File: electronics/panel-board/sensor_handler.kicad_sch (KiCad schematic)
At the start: 23 parts, among them J1 Load Cell Input, J2 FSR Input, J3 Digital Input, U1 LMV321, U2 INA826

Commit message: Pre LED grid changes
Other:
- note added: "Instrumentation Amplifier for Load Cell Sensor (Typically GML 670, 50kg) - 1kHz cut-off DM filtering. 330x gain. Rail-to-rail output. 470R resistor prevents internal saturation in first stage of inamp due to non rail-to-rail performance internally with CM amplification."
- note removed: "Instrumentation Amplifier for Load Cell Sensor (Typically GML 670, 50kg) - 1kHz cut-off CM/DM filtering. 330x gain. Rail-to-rail output. 470R resistor prevents internal saturation in first stage of inamp due to non rail-to-rail performance internally with CM amplification."
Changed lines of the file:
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@@
     (effects (font (size 1.27 1.27)) (justify left bottom))
   )
-  (text "Instrumentation Amplifier for Load Cell Sensor (Typically GML 670, 50kg) - 1kHz cut-off CM/DM filtering. 330x gain. Rail-to-rail output.\n470R resistor prevents internal saturation in first stage of inamp due to non rail-to-rail performance internally with CM amplification."
+  (text "Instrumentation Amplifier for Load Cell Sensor (Typically GML 670, 50kg) - 1kHz cut-off DM filtering. 330x gain. Rail-to-rail output.\n470R resistor prevents internal saturation in first stage of inamp due to non rail-to-rail performance internally with CM amplification."
     (at 16.51 19.05 0)
     (effects (font (size 1.27 1.27)) (justify left bottom))

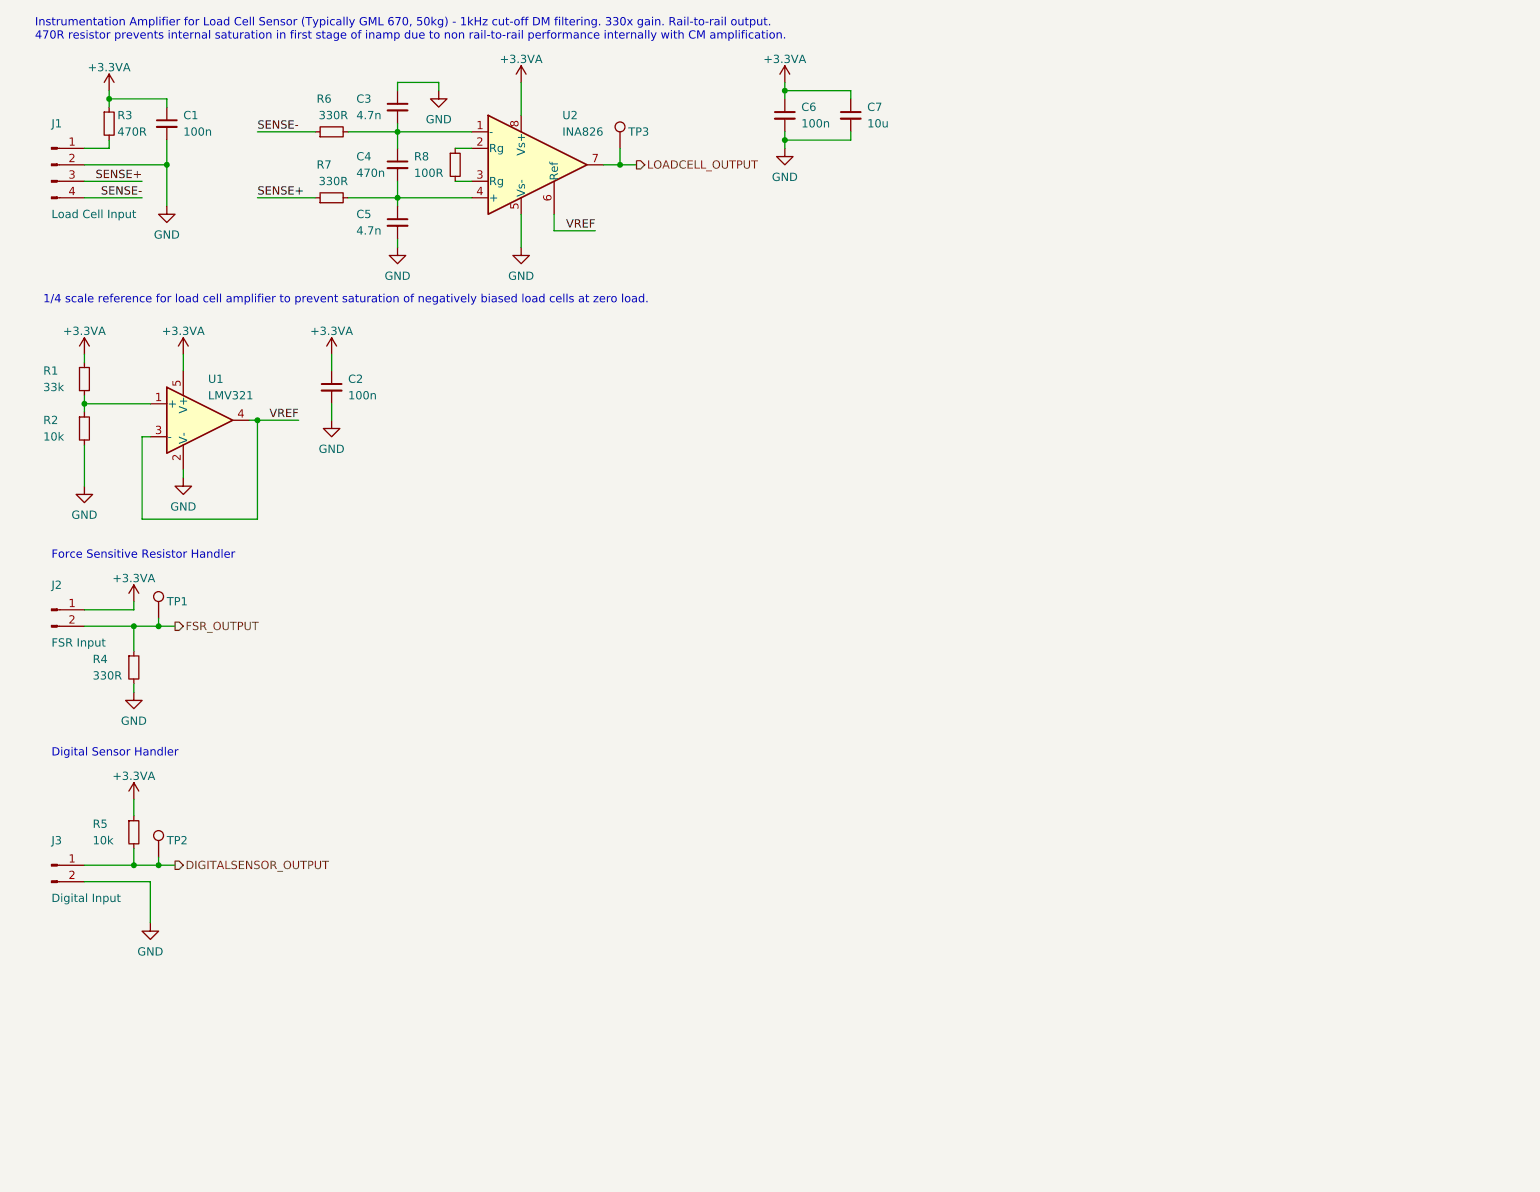
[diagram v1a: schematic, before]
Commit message: Prelim schematic for FSR+LC gain/adj dig control
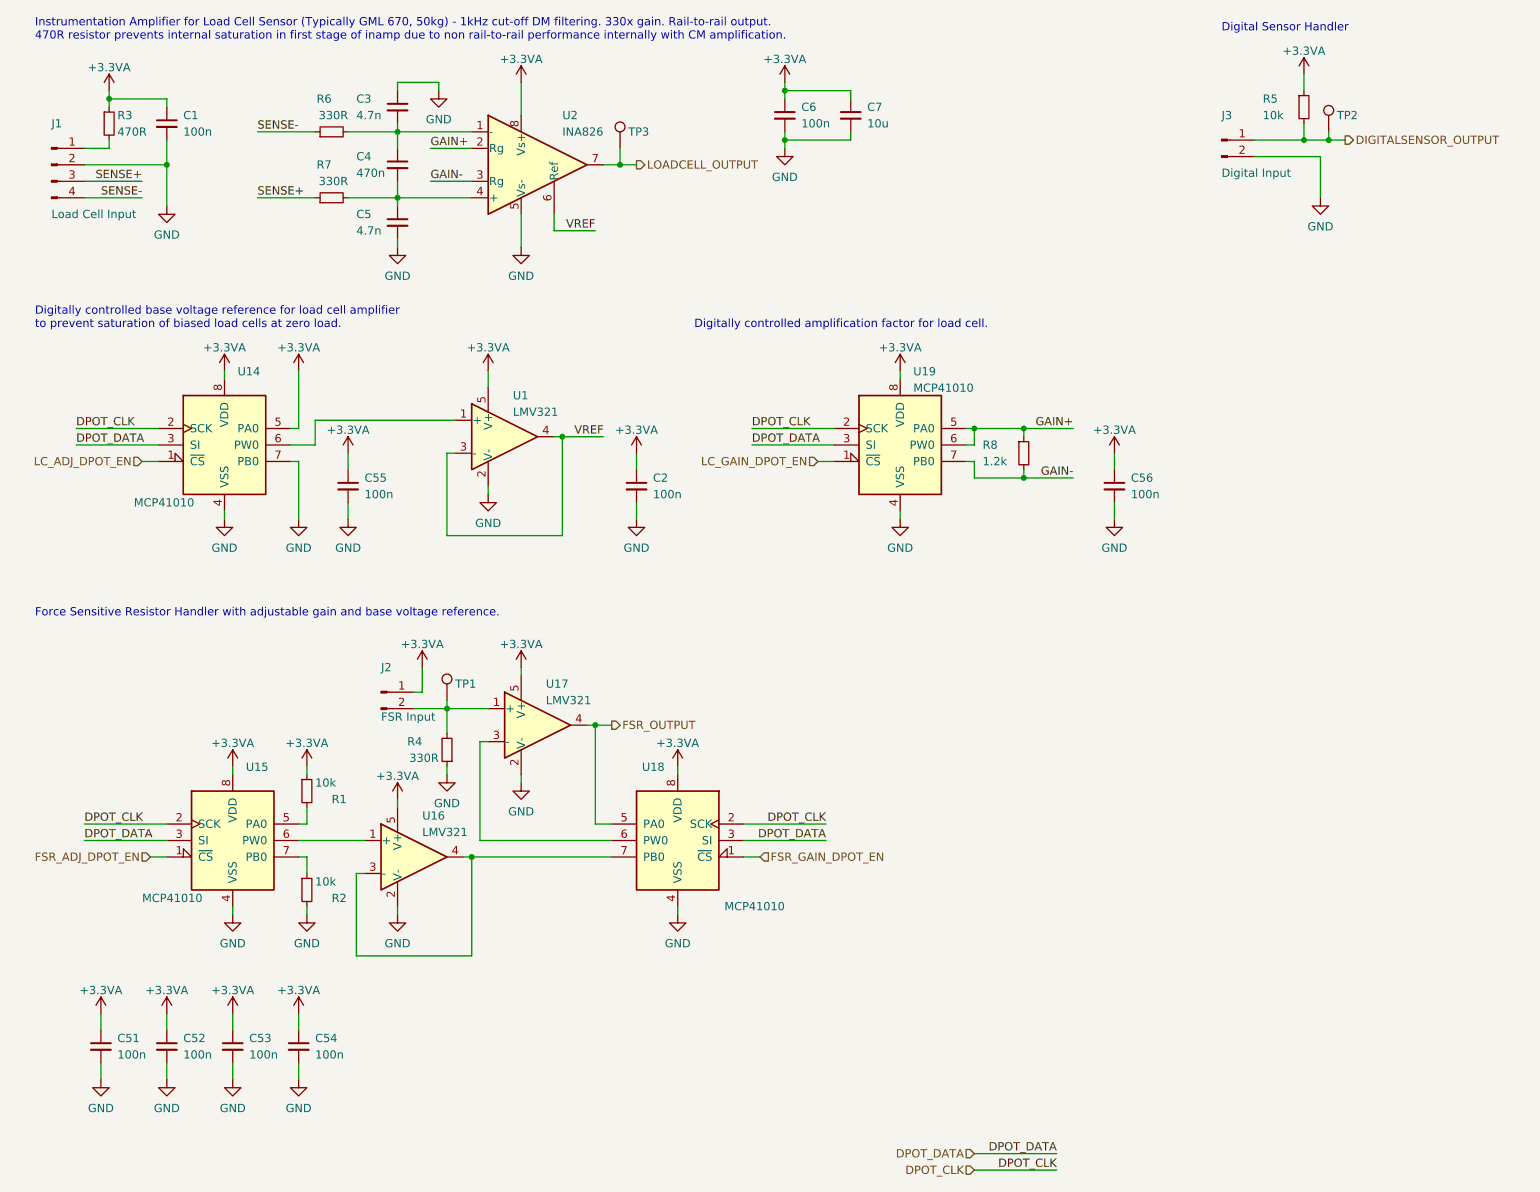
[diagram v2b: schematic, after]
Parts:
- added C51, C52, C53, C54, C55, C56: 100n, Capacitor_SMD:C_0603_1608Metric, symbol Device:C_Small
- added U14, U15, U18, U19: MCP41010, Package_SO:SOIC-8_3.9x4.9mm_P1.27mm, symbol Potentiometer_Digital:MCP41010
- added U16, U17: LMV321, Package_TO_SOT_SMD:SOT-23-5, symbol Amplifier_Operational:LMV321
- R1: value 33k -> 10k
- R8: value 100R -> 1.2k
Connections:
- net +3.3VA: now also C51.1, C52.1, C53.1, C54.1, C55.1, C56.1, U14.5 (PA0), U14.8 (VDD), U15.8 (VDD), U16.5 (V+), U17.5 (V+), U18.8 (VDD), U19.8 (VDD)
- net FSR_OUTPUT: now also U17.4, U18.5 (PA0); no longer J2.2 (Pin_2), R4.1, TP1.1
- net GND: now also R4.1, C51.2, C52.2, C53.2, C54.2, C55.2, C56.2, U14.4 (VSS), U14.7 (PB0), U15.4 (VSS), U16.2 (V-), U17.2 (V-), U18.4 (VSS), U19.4 (VSS); no longer R4.2
- net GAIN+: now reaches R8.1, U2.2 (Rg)
- net GAIN+: now also U19.5 (PA0), U19.6 (PW0)
- net GAIN-: now reaches R8.2, U2.3 (Rg)
- net GAIN-: now also U19.7 (PB0)
- new net: J2.2 (Pin_2), R4.2, TP1.1, U17.1 (+)
- new net: U15.6 (PW0), U16.1 (+)
- new net: U16.3 (-), U16.4, U18.7 (PB0)
- new net: U1.1 (+), U14.6 (PW0)
- new net: R1.2, U15.5 (PA0)
- new net: R2.1, U15.7 (PB0)
- new net: U17.3 (-), U18.6 (PW0)
- new net DPOT_CLK: U14.2 (SCK), U15.2 (SCK), U18.2 (SCK), U19.2 (SCK)
- new net DPOT_DATA: U14.3 (SI), U15.3 (SI), U18.3 (SI), U19.3 (SI)
- new net FSR_ADJ_DPOT_EN: U15.1 (~{CS})
- new net FSR_GAIN_DPOT_EN: U18.1 (~{CS})
- new net LC_ADJ_DPOT_EN: U14.1 (~{CS})
- new net LC_GAIN_DPOT_EN: U19.1 (~{CS})
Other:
- note added: "Digitally controlled amplification factor for load cell."
- note added: "Digitally controlled base voltage reference for load cell amplifier to prevent saturation of biased load cells at zero load."
- note added: "Force Sensitive Resistor Handler with adjustable gain and base voltage reference."
- note removed: "1/4 scale reference for load cell amplifier to prevent saturation of negatively biased load cells at zero load."
- note removed: "Force Sensitive Resistor Handler"
- moved on the sheet: C2, J3, R5, TP2, U1
